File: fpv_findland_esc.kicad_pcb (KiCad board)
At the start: 6 copper layers, 36 x 47.4 mm, 157 parts, among them J1 Conn_01x01_Pin, J10 Conn_01x01_Pin, J11 Conn_01x01_Pin, J12 Conn_01x01_Pin, J13 Conn_01x01_Pin, J2 Conn_01x06, J3 Conn_01x01_Pin, J4 Conn_01x01_Pin, J5 Conn_01x01_Pin, J6 Conn_01x01_Pin, J7 Conn_01x01_Pin, J8 Conn_01x01_Pin, J9 Conn_01x01_Pin, Q1 FDMC8010DC, Q10 FDMC8010DC, Q11 FDMC8010DC, Q12 FDMC8010DC, Q13 FDMC8010DC, Q14 FDMC8010DC, Q15 FDMC8010DC, Q16 FDMC8010DC, Q17 FDMC8010DC, Q18 FDMC8010DC, Q19 FDMC8010DC, Q2 FDMC8010DC, Q20 FDMC8010DC, Q21 FDMC8010DC, Q22 FDMC8010DC, Q23 FDMC8010DC, Q24 FDMC8010DC, Q3 FDMC8010DC, Q4 FDMC8010DC, Q5 FDMC8010DC, Q6 FDMC8010DC, Q7 FDMC8010DC, Q8 FDMC8010DC, Q9 FDMC8010DC, U1 GD32E230G8U6, U10 DRV8300D, U2 WL2851E33, U3 GD32E230G8U6, U4 GD32E230G8U6, U5 ST732M50R, U6 GD32E230G8U6, U7 DRV8300D, U8 DRV8300D, U9 DRV8300D

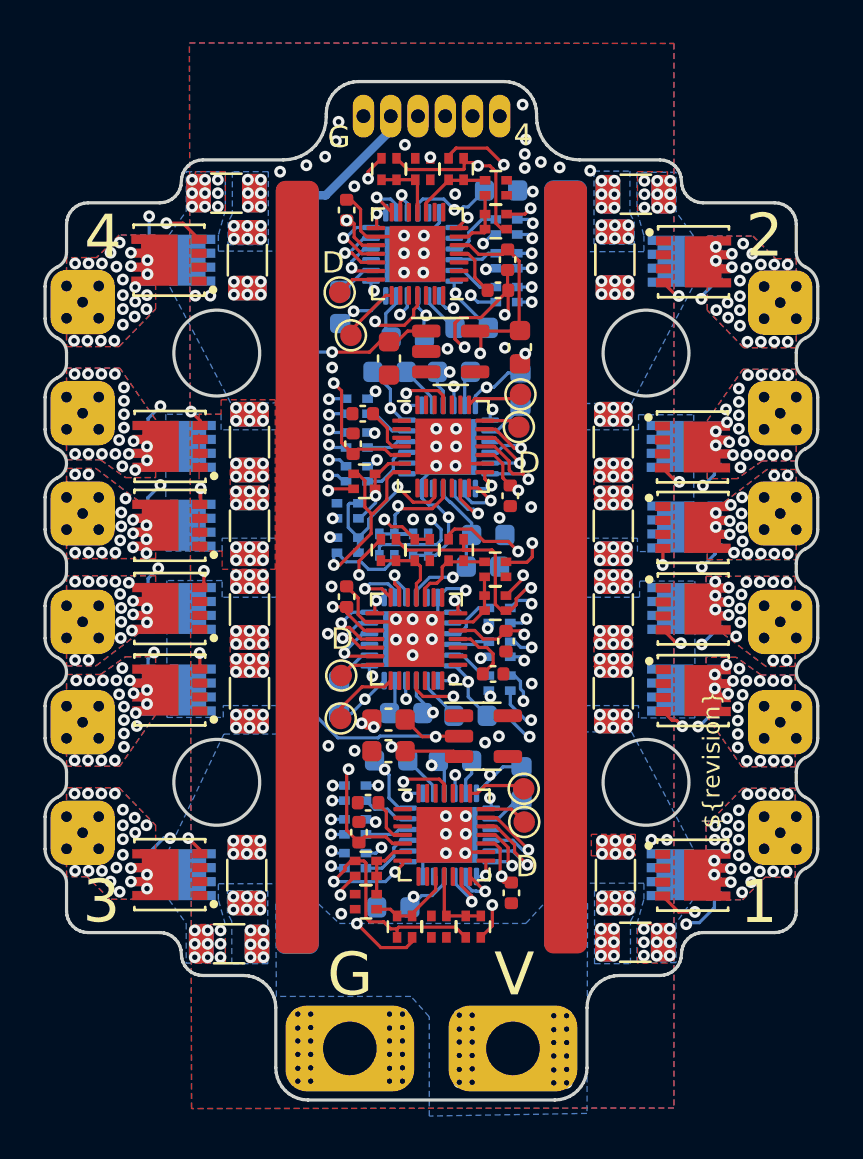
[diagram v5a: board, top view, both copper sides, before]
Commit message: Updated power supply scheme. 10V step down to a 3.3V LDO.
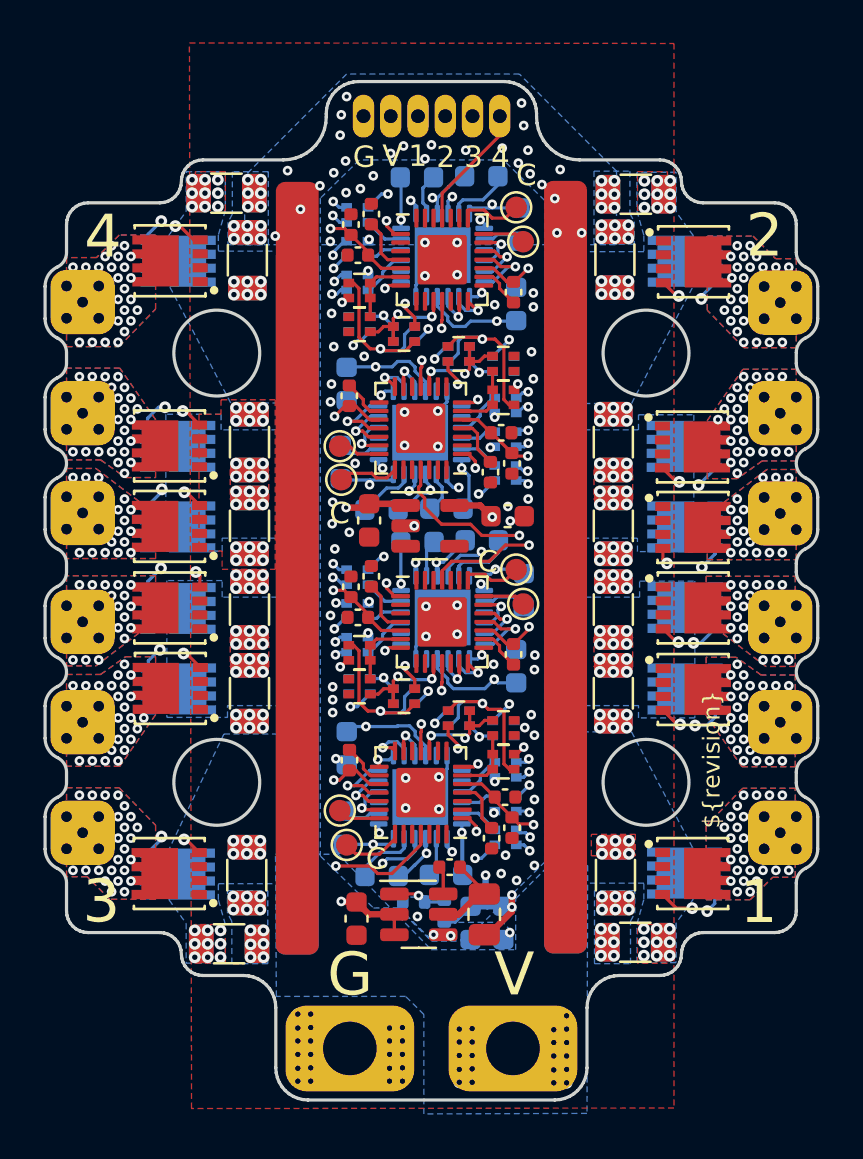
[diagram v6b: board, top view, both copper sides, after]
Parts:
- added C65: 100nF, Capacitor_SMD:C_0402_1005Metric, F.Cu at (136.3, 89.0)
- added C66: 10uF, Capacitor_SMD:C_0603_1608Metric, B.Cu at (138.8, 91.5)
- added C67: 10uF, Capacitor_SMD:C_0603_1608Metric, B.Cu at (137.3, 91.5)
- added C68: 10uF, Capacitor_SMD:C_0603_1608Metric, F.Cu at (132.0, 91.3)
- added C69: 1uF, Capacitor_SMD:C_0402_1005Metric, F.Cu at (139.2, 70.1)
- added C70: 1uF, Capacitor_SMD:C_0402_1005Metric, F.Cu at (139.3, 87.1)
- added L1: 10uF, Capacitor_SMD:C_0805_2012Metric, F.Cu at (138.0, 91.2)
- added R1: 20K, Resistor_SMD:R_0402_1005Metric, B.Cu at (134.7, 90.6)
- added R2: 230K, Resistor_SMD:R_0402_1005Metric, B.Cu at (136.1, 91.0)
- C18, C9: value 10uF -> 1uF; footprint Capacitor_SMD:C_0603_1608Metric -> Capacitor_SMD:C_0402_1005Metric
- RN10, RN12, RN16, RN3, RN4, RN7: moved to B.Cu
- RN20, RN22: moved to F.Cu
- U5: value ST732M50R -> AP63200; footprint OpenHW:SOT-23-5 -> OpenHW:SOT-23-6
- moved C28 14.7 mm to (132.1, 77.3), turned to 180 degrees
- moved C62 12.6 mm to (139.4, 79.6), turned to 90 degrees
- moved C15 11.9 mm to (138.9, 85.7), turned to 0 degrees
- moved RN12 11.8 mm to (132.2, 80.5), turned to 180 degrees
- moved C38 11.5 mm to (131.6, 66.4), turned to -90 degrees
- moved RN16 11.2 mm to (134.2, 81.0), turned to 0 degrees
- moved C14 11.0 mm to (139.3, 79.0), turned to -90 degrees
- moved C52 10.8 mm to (139.4, 62.7), turned to 90 degrees
- moved RN15 10.7 mm to (134.2, 81.0), turned to 0 degrees
- moved RN24 10.7 mm to (132.2, 63.6), turned to 180 degrees
- moved C59 10.6 mm to (131.6, 83.4), turned to -90 degrees
- moved C21 10.5 mm to (132.7, 75.4), turned to 90 degrees
- moved C57 10.4 mm to (137.8, 73.7)
- moved C48 10.2 mm to (134.8, 73.8)
- moved TP10 10.2 mm to (139.4, 75.1), turned to 180 degrees
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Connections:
- net /Motor1/AHIGH renamed /ESC3/AHIGH
- net /Motor1/ALOW renamed /ESC3/ALOW
- net /Motor1/BEMFA_1 renamed /ESC3/BEMFA_1
- net /Motor1/BEMFB_1 renamed /ESC3/BEMFB_1
- net /Motor1/BEMFC_1 renamed /ESC3/BEMFC_1
- net /Motor1/BEMF_COMMON renamed /ESC3/BEMF_COMMON
- net /Motor1/BHIGH renamed /ESC3/BHIGH
- net /Motor1/BLOW renamed /ESC3/BLOW
- net /Motor1/CHIGH renamed /ESC3/CHIGH
- net /Motor1/CLOW renamed /ESC3/CLOW
- net /Motor1/GHA renamed /ESC3/GHA
- net /Motor1/GHB renamed /ESC3/GHB
- net /Motor1/GHC renamed /ESC3/GHC
- net /Motor1/GLA renamed /ESC3/GLA
- net /Motor1/GLB renamed /ESC3/GLB
- net /Motor1/GLC renamed /ESC3/GLC
- net /Motor1/MotorOutA renamed /ESC3/MotorOutA
- net /Motor1/MotorOutB renamed /ESC3/MotorOutB
- net /Motor1/MotorOutC renamed /ESC3/MotorOutC
- net /Motor1/SWC renamed /ESC3/SWC
- net /Motor1/SWD renamed /ESC3/SWD
- net /Motor1/V_SENSE renamed /ESC3/V_SENSE
- net /Motor2/AHIGH renamed /ESC4/AHIGH
- net /Motor2/ALOW renamed /ESC4/ALOW
- net /Motor2/BEMFA_1 renamed /ESC4/BEMFA_1
- net /Motor2/BEMFB_1 renamed /ESC4/BEMFB_1
- net /Motor2/BEMFC_1 renamed /ESC4/BEMFC_1
- net /Motor2/BEMF_COMMON renamed /ESC4/BEMF_COMMON
- net /Motor2/BHIGH renamed /ESC4/BHIGH
- net /Motor2/BLOW renamed /ESC4/BLOW
- net /Motor2/CHIGH renamed /ESC4/CHIGH
- net /Motor2/CLOW renamed /ESC4/CLOW
- net /Motor2/GHA renamed /ESC4/GHA
- net /Motor2/GHB renamed /ESC4/GHB
- net /Motor2/GHC renamed /ESC4/GHC
- net /Motor2/GLA renamed /ESC4/GLA
- net /Motor2/GLB renamed /ESC4/GLB
- net /Motor2/GLC renamed /ESC4/GLC
- net /Motor2/MotorOutA renamed /ESC4/MotorOutA
- net /Motor2/MotorOutB renamed /ESC4/MotorOutB
- net /Motor2/MotorOutC renamed /ESC4/MotorOutC
- net /Motor2/SWC renamed /ESC4/SWC
- net /Motor2/SWD renamed /ESC4/SWD
- net /Motor2/V_SENSE renamed /ESC4/V_SENSE
- net /Motor3/AHIGH renamed /ESC2/AHIGH
- net /Motor3/ALOW renamed /ESC2/ALOW
- net /Motor3/BEMFA_1 renamed /ESC2/BEMFA_1
- net /Motor3/BEMFB_1 renamed /ESC2/BEMFB_1
- net /Motor3/BEMFC_1 renamed /ESC2/BEMFC_1
- net /Motor3/BEMF_COMMON renamed /ESC2/BEMF_COMMON
- net /Motor3/BHIGH renamed /ESC2/BHIGH
- net /Motor3/BLOW renamed /ESC2/BLOW
- net /Motor3/CHIGH renamed /ESC2/CHIGH
- net /Motor3/CLOW renamed /ESC2/CLOW
- net /Motor3/GHA renamed /ESC2/GHA
- net /Motor3/GHB renamed /ESC2/GHB
- net /Motor3/GHC renamed /ESC2/GHC
- net /Motor3/GLA renamed /ESC2/GLA
- net /Motor3/GLB renamed /ESC2/GLB
- net /Motor3/GLC renamed /ESC2/GLC
- net /Motor3/MotorOutA renamed /ESC2/MotorOutA
- net /Motor3/MotorOutB renamed /ESC2/MotorOutB
- net /Motor3/MotorOutC renamed /ESC2/MotorOutC
- net /Motor3/SWC renamed /ESC2/SWC
- net /Motor3/SWD renamed /ESC2/SWD
- net /Motor3/V_SENSE renamed /ESC2/V_SENSE
- net /Motor4/AHIGH renamed /ESC1/AHIGH
- net /Motor4/ALOW renamed /ESC1/ALOW
- net /Motor4/BEMFA_1 renamed /ESC1/BEMFA_1
- net /Motor4/BEMFB_1 renamed /ESC1/BEMFB_1
- net /Motor4/BEMFC_1 renamed /ESC1/BEMFC_1
- net /Motor4/BEMF_COMMON renamed /ESC1/BEMF_COMMON
- net /Motor4/BHIGH renamed /ESC1/BHIGH
- net /Motor4/BLOW renamed /ESC1/BLOW
- net /Motor4/CHIGH renamed /ESC1/CHIGH
- net /Motor4/CLOW renamed /ESC1/CLOW
- net /Motor4/GHA renamed /ESC1/GHA
- net /Motor4/GHB renamed /ESC1/GHB
- net /Motor4/GHC renamed /ESC1/GHC
- net /Motor4/GLA renamed /ESC1/GLA
- net /Motor4/GLB renamed /ESC1/GLB
- net /Motor4/GLC renamed /ESC1/GLC
- net /Motor4/MotorOutA renamed /ESC1/MotorOutA
- net /Motor4/MotorOutB renamed /ESC1/MotorOutB
- net /Motor4/MotorOutC renamed /ESC1/MotorOutC
- net /Motor4/SWC renamed /ESC1/SWC
- net /Motor4/SWD renamed /ESC1/SWD
- net /Motor4/V_SENSE renamed /ESC1/V_SENSE
- C17 pad 1: /VBAT -> /5V
- C18 pad 1: /VBAT -> /3.3V
- C9 pad 1: /5V -> /3.3V
- RN10 pad 2: unconnected-(RN29-R2.1-Pad2) -> /ESC1/Boot0
- RN12 pad 2: unconnected-(RN8-R2.1-Pad2) -> /ESC3/Boot0
- RN24 pad 2: unconnected-(RN13-R2.1-Pad2) -> /ESC4/Boot0
- RN3 pad 2: unconnected-(RN21-R2.1-Pad2) -> /ESC2/Boot0
- U1 pad 1: unconnected-(U5-BOOT0-Pad1) -> /ESC2/Boot0
- U2 pad 1: /VBAT -> /5V
- U3 pad 1: unconnected-(U1-BOOT0-Pad1) -> /ESC3/Boot0
- U4 pad 1: unconnected-(U7-BOOT0-Pad1) -> /ESC1/Boot0
- U5 pad 1: GND -> Net-(U5-FB)
- U5 pad 3: /5V -> /VBAT
- U5 pad 4: (no net) -> GND
- U5 pad 5: (no net) -> Net-(U5-SW)
- U6 pad 1: unconnected-(U3-BOOT0-Pad1) -> /ESC4/Boot0
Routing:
- net /VBAT: track 90.6 -> 14.9 mm, vias 134 -> 130
- net GND: track 34.2 -> 12.7 mm, vias 187 -> 202
- net /M4: track 24.2 -> 5.86 mm, vias 1 -> 0
- net /M3: track 44.5 -> 26.6 mm, vias 2 -> 1
- net /M2: track 15.9 -> 29.8 mm
- net /ESC2/Boot0: track 0.00 -> 8.82 mm, vias 0 -> 2
- net Net-(Q24-G): track 11.2 -> 20.0 mm
- net /ESC1/Boot0: track 0.00 -> 8.73 mm, vias 0 -> 2
- net /ESC3/Boot0: track 0.00 -> 8.68 mm, vias 0 -> 2
- net /ESC4/Boot0: track 0.00 -> 8.62 mm, vias 0 -> 2
- net Net-(Q11-G): track 9.60 -> 18.1 mm
- net /5V: track 73.0 -> 81.5 mm, vias 4 -> 8
- net Net-(Q17-G): track 20.3 -> 12.2 mm
- net /ESC4/MotorOutC: track 29.1 -> 37.1 mm
- net Net-(Q7-G): track 17.8 -> 9.96 mm
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- added copper zone on In1.Cu, net /VBAT
- added copper zone on In1.Cu, net GND
- removed copper zone on In2.Cu, net /VBAT
- removed copper zone on In2.Cu, net GND
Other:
- board text added: "C"
- board text removed: "D"

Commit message: Removed unneccessary islands etc.
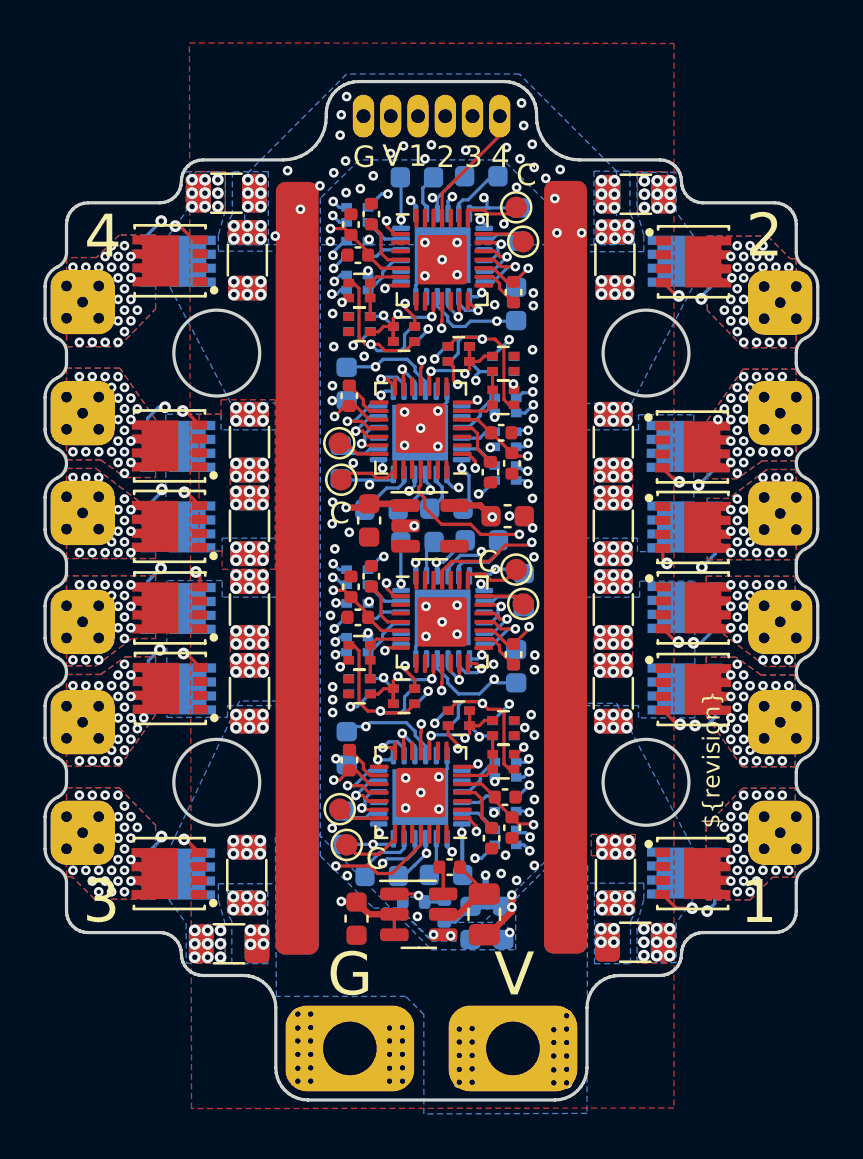
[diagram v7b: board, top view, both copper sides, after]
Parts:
- TP13, TP14: footprint OpenHW:2mmBussBar -> OpenHW:2mmBussBar33MM
- TP4, TP9: footprint OpenHW:2mmBussBar -> OpenHW:2mmBussBar36MM
- moved TP1 0.14 mm to (131.2, 69.2)
- moved TP7 0.07 mm to (131.2, 86.2)
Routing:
- net /ESC2/MotorOutA: track 32.1 -> 34.6 mm
- net /ESC4/MotorOutC: track 37.1 -> 39.3 mm
- net /ESC1/MotorOutC: track 35.4 -> 36.7 mm
- net /5V: track 81.5 -> 80.3 mm
- net /M2: track 29.8 -> 29.2 mm
- net /ESC2/MotorOutC: track 35.4 -> 35.6 mm, vias 26 -> 28
- net /ESC3/MotorOutC: track 38.7 -> 38.8 mm, vias 26 -> 28
- net GND: vias 202 -> 207
